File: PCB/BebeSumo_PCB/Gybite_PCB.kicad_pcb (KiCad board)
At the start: 2 copper layers, 77.7 x 36.4 mm, 15 parts, among them J1 Pulsador, J10 JSUMO, J11 Sharps, J12 Conector Batería, J2 Motor 1, J3 HC-SR04, J4 Motor 2, J5 QRE1113, J6 QRE1113, J7 Arduino_Nano_Header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

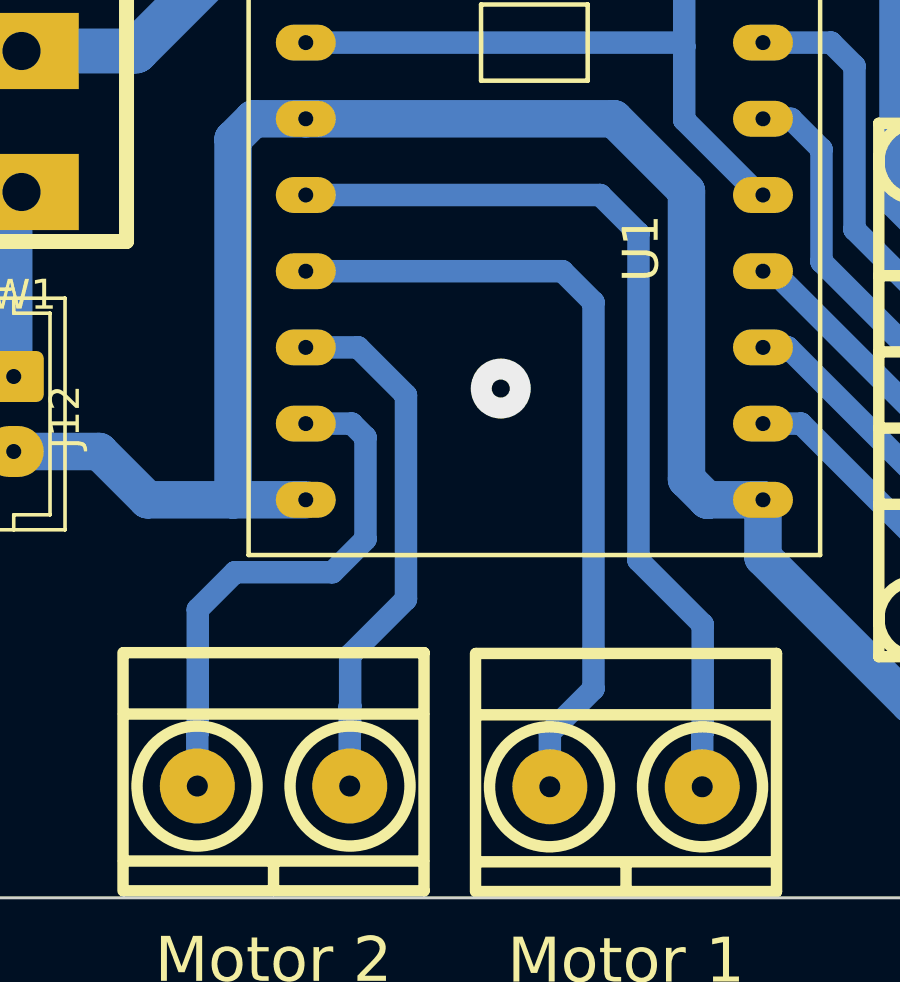
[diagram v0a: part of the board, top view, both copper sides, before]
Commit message: Agregue debug a las acciones dentro de las estrategias.
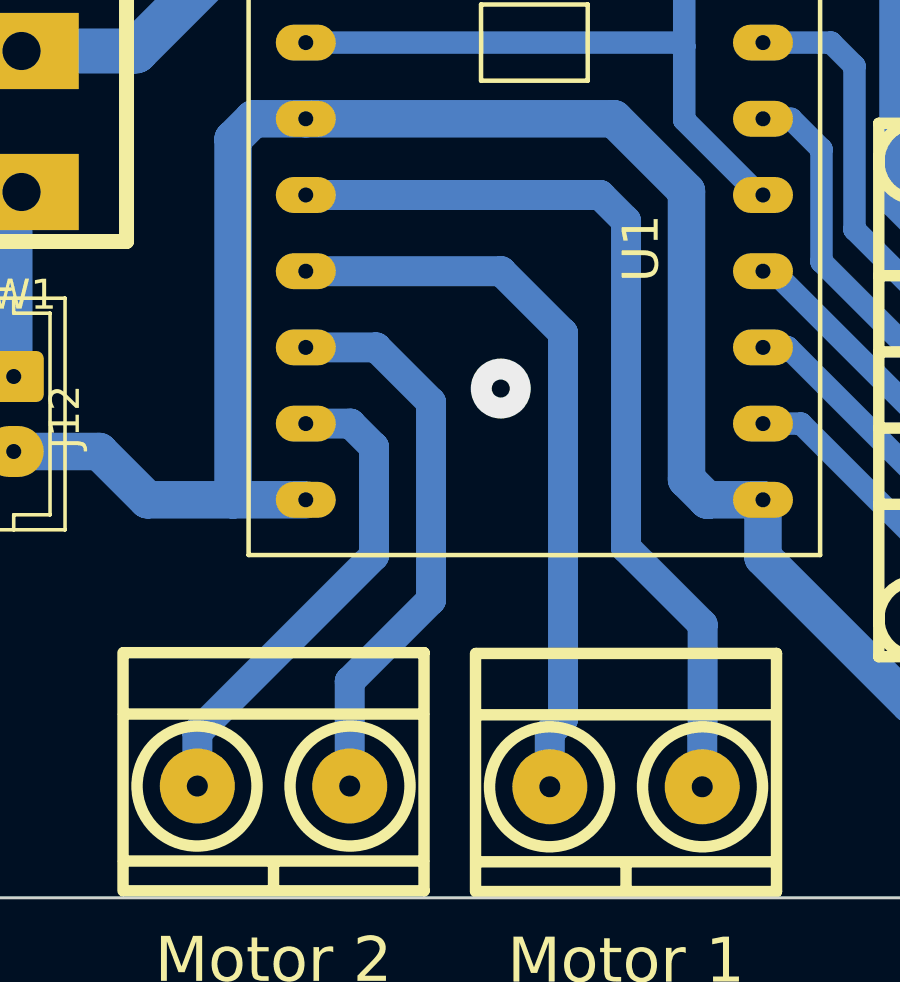
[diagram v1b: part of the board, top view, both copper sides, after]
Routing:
- net /Motor 1B: track 26.8 -> 24.7 mm
- net /Motor 2B: track 18.0 -> 16.3 mm
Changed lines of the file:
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@@
   (segment (start 173.84 82.67375) (end 167.44 82.67375) (width 0.75) (layer "B.Cu") (net 4))
   (segment (start 123.1 99.95875) (end 123.1 87.93875) (width 1.25) (layer "B.Cu") (net 4))
-  (segment (start 136.615 91.07375) (end 136.615 101.97375) (width 0.75) (layer "B.Cu") (net 5))
-  (segment (start 136.615 101.97375) (end 138.755 104.11375) (width 0.75) (layer "B.Cu") (net 5))
-  (segment (start 138.74 107.715) (end 138.74 109.525) (width 0.75) (layer "B.Cu") (net 5))
-  (segment (start 125.525 89.79875) (end 135.34 89.79875) (width 0.75) (layer "B.Cu") (net 5))
-  (segment (start 138.755 107.7) (end 138.74 107.715) (width 0.75) (layer "B.Cu") (net 5))
-  (segment (start 135.34 89.79875) (end 136.615 91.07375) (width 0.75) (layer "B.Cu") (net 5))
-  (segment (start 138.755 104.11375) (end 138.755 107.7) (width 0.75) (layer "B.Cu") (net 5))
-  (segment (start 125.525 92.33875) (end 134.08 92.33875) (width 0.75) (layer "B.Cu") (net 6))
-  (segment (start 134.08 92.33875) (end 135.115 93.37375) (width 0.75) (layer "B.Cu") (net 6))
-  (segment (start 135.115 106.26) (end 133.66 107.715) (width 0.75) (layer "B.Cu") (net 6))
-  (segment (start 135.115 93.37375) (end 135.115 106.26) (width 0.75) (layer "B.Cu") (net 6))
-  (segment (start 133.66 107.715) (end 133.66 109.525) (width 0.75) (layer "B.Cu") (net 6))
+  (segment (start 125.525 89.79875) (end 135.34 89.79875) (width 1) (layer "B.Cu") (net 5))
+  (segment (start 135.34 89.79875) (end 136.2 90.65875) (width 1) (layer "B.Cu") (net 5))
+  (segment (start 136.2 101.55875) (end 138.755 104.11375) (width 1) (layer "B.Cu") (net 5))
+  (segment (start 138.755 104.11375) (end 138.755 107.7) (width 1) (layer "B.Cu") (net 5))
+  (segment (start 136.2 90.65875) (end 136.2 101.55875) (width 1) (layer "B.Cu") (net 5))
+  (segment (start 138.755 107.7) (end 138.74 107.715) (width 1) (layer "B.Cu") (net 5))
+  (segment (start 138.74 107.715) (end 138.74 109.525) (width 1) (layer "B.Cu") (net 5))
+  (segment (start 134.1 107.275) (end 133.66 107.715) (width 1) (layer "B.Cu") (net 6))
+  (segment (start 125.525 92.33875) (end 132.03875 92.33875) (width 1) (layer "B.Cu") (net 6))
+  (segment (start 132.03875 92.33875) (end 134.1 94.4) (width 1) (layer "B.Cu") (net 6))
+  (segment (start 134.1 94.4) (end 134.1 107.275) (width 1) (layer "B.Cu") (net 6))
+  (segment (start 133.66 107.715) (end 133.66 109.525) (width 1) (layer "B.Cu") (net 6))
   (segment (start 156.055 88.67875) (end 156.055 90.88875) (width 0.75) (layer "B.Cu") (net 7))
   (segment (start 185.675 105.825) (end 186.425 105.075) (width 0.75) (layer "B.Cu") (net 7))
@@
   (segment (start 176.375 103.91875) (end 176.375 104.125) (width 0.75) (layer "B.Cu") (net 9))
   (segment (start 176.375 104.125) (end 180.675 108.425) (width 0.75) (layer "B.Cu") (net 9))
-  (segment (start 125.525 94.87875) (end 127.27 94.87875) (width 0.75) (layer "B.Cu") (net 10))
-  (segment (start 128.865 96.47375) (end 128.865 103.27375) (width 0.75) (layer "B.Cu") (net 10))
-  (segment (start 128.865 103.27375) (end 127.005 105.13375) (width 0.75) (layer "B.Cu") (net 10))
-  (segment (start 127.27 94.87875) (end 128.865 96.47375) (width 0.75) (layer "B.Cu") (net 10))
-  (segment (start 127.005 105.13375) (end 127.005 106.83) (width 0.75) (layer "B.Cu") (net 10))
-  (segment (start 126.99 109.5) (end 126.99 106.845) (width 0.75) (layer "B.Cu") (net 10))
-  (segment (start 127.005 106.83) (end 127.005 107.7) (width 0.75) (layer "B.Cu") (net 10))
-  (segment (start 126.99 106.845) (end 127.005 106.83) (width 0.75) (layer "B.Cu") (net 10))
-  (segment (start 127.515 101.27375) (end 126.415 102.37375) (width 0.75) (layer "B.Cu") (net 11))
-  (segment (start 121.925 103.61375) (end 121.925 107.7) (width 0.75) (layer "B.Cu") (net 11))
-  (segment (start 126.415 102.37375) (end 123.165 102.37375) (width 0.75) (layer "B.Cu") (net 11))
-  (segment (start 127.06 97.41875) (end 127.515 97.87375) (width 0.75) (layer "B.Cu") (net 11))
-  (segment (start 123.165 102.37375) (end 121.925 103.61375) (width 0.75) (layer "B.Cu") (net 11))
-  (segment (start 125.525 97.41875) (end 127.06 97.41875) (width 0.75) (layer "B.Cu") (net 11))
-  (segment (start 127.515 97.87375) (end 127.515 101.27375) (width 0.75) (layer "B.Cu") (net 11))
-  (segment (start 121.91 107.715) (end 121.925 107.7) (width 0.75) (layer "B.Cu") (net 11))
-  (segment (start 121.91 109.5) (end 121.91 107.715) (width 0.75) (layer "B.Cu") (net 11))
+  (segment (start 126.99 106.01) (end 126.99 109.5) (width 1) (layer "B.Cu") (net 10))
+  (segment (start 125.525 94.87875) (end 127.874375 94.87875) (width 1) (layer "B.Cu") (net 10))
+  (segment (start 129.7 103.3) (end 126.99 106.01) (width 1) (layer "B.Cu") (net 10))
+  (segment (start 129.7 96.704375) (end 129.7 103.3) (width 1) (layer "B.Cu") (net 10))
+  (segment (start 127.874375 94.87875) (end 129.7 96.704375) (width 1) (layer "B.Cu") (net 10))
+  (segment (start 127.01875 97.41875) (end 127.8 98.2) (width 1) (layer "B.Cu") (net 11))
+  (segment (start 127.8 98.2) (end 127.8 101.825) (width 1) (layer "B.Cu") (net 11))
+  (segment (start 125.525 97.41875) (end 127.01875 97.41875) (width 1) (layer "B.Cu") (net 11))
+  (segment (start 127.8 101.825) (end 121.91 107.715) (width 1) (layer "B.Cu") (net 11))
+  (segment (start 121.91 107.715) (end 121.91 109.5) (width 1) (layer "B.Cu") (net 11))
   (segment (start 183.75125 85.22375) (end 182.125 86.85) (width 0.75) (layer "B.Cu") (net 12))
   (segment (start 176.375 87.5) (end 176.375 88.67875) (width 0.75) (layer "B.Cu") (net 12))
